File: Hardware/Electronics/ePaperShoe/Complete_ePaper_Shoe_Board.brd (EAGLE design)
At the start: 160 x 100 mm, 59 parts, among them Q1 IRF7509, U1 LM3671MF-3.3/NOPB, U2 NRF52832, U3 MCP73871, X1 32MHz, X2 32.768kHz, X3 FH12-26S-0.5SH

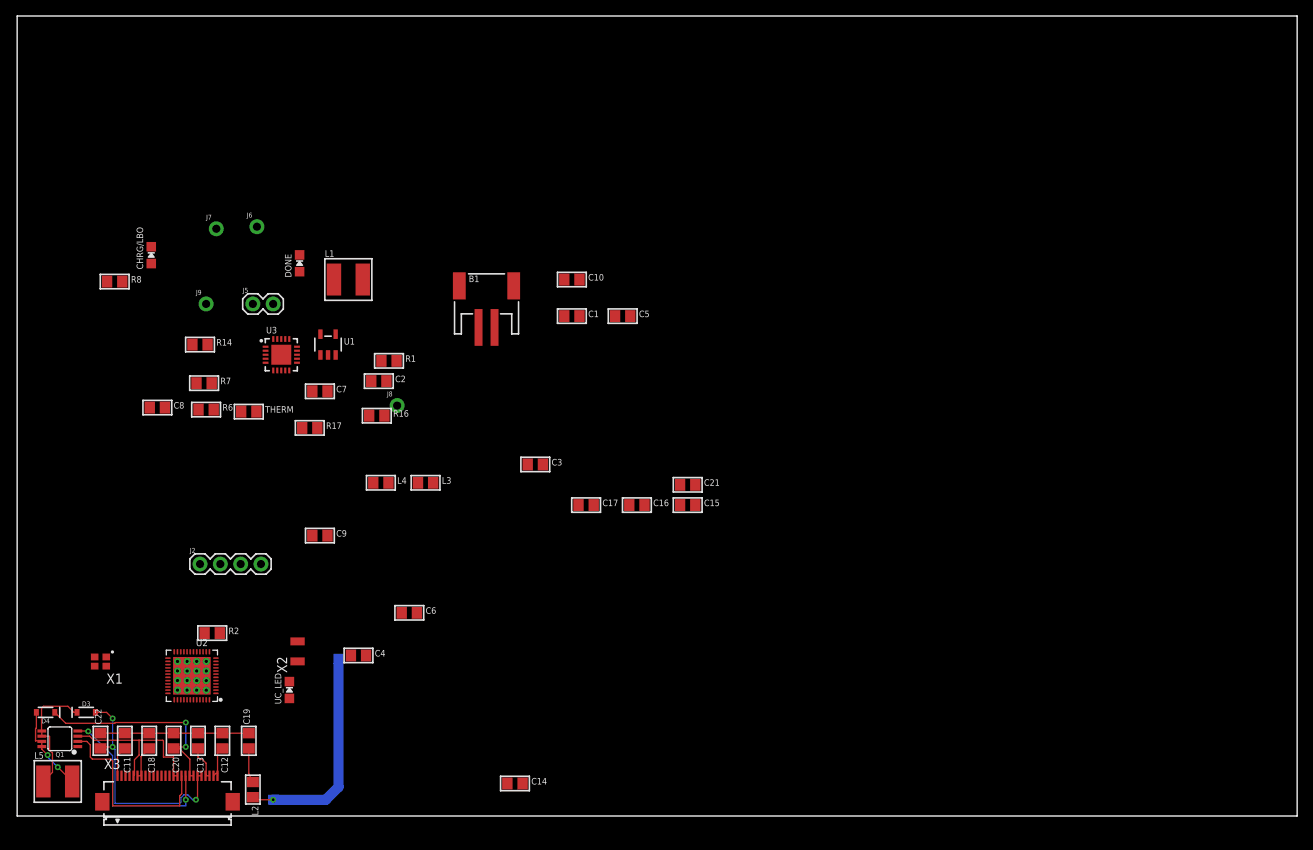
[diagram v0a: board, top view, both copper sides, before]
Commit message: Completed layout and traces of PCB. Need to still add silkscreen and arrange lables
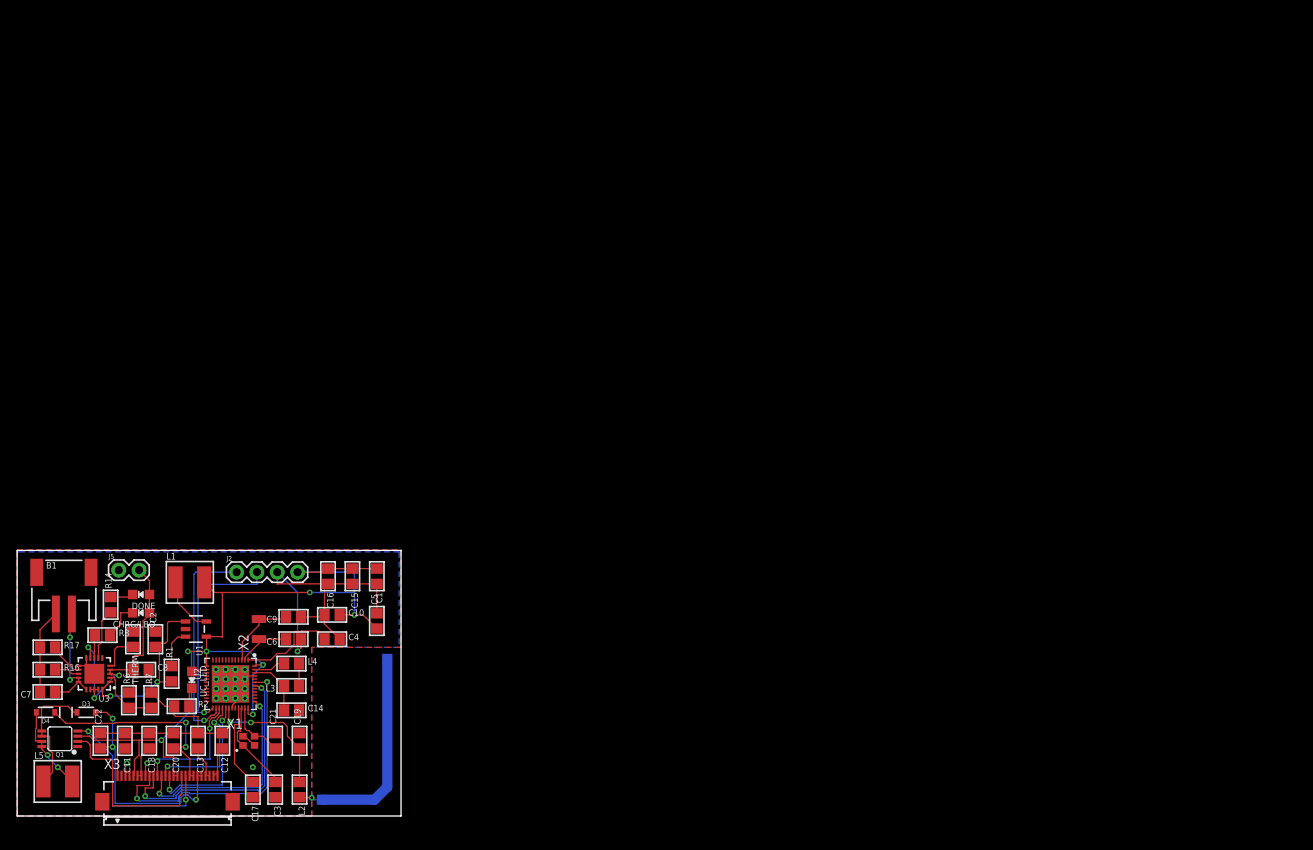
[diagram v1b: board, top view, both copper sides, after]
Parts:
- removed J6, J7, J8, J9: (no value), SparkFun-Connectors:1X01_NO_SILK
- moved FRAME1 81.9 mm to (-4.32, 23.1)
- moved B1 63.8 mm to (5.84, 29.0)
- moved C21 60.7 mm to (32.3, 9.40), turned to 90 degrees
- moved C17 54.8 mm to (29.5, 3.30), turned to 270 degrees
- moved C3 52.0 mm to (32.3, 3.30), turned to 270 degrees
- moved R16 52.0 mm to (3.81, 18.3)
- moved C10 51.5 mm to (39.4, 25.1)
- moved C7 50.7 mm to (3.81, 15.5), turned to 180 degrees
- moved C5 49.0 mm to (45.0, 24.4), turned to 90 degrees
- moved R1 47.6 mm to (19.3, 17.8), turned to 90 degrees
- moved U3 46.2 mm to (9.65, 17.8), turned to 180 degrees
- moved DONE 45.9 mm to (15.5, 27.7), turned to 90 degrees
- moved CHRG/LBO 44.7 mm to (15.5, 25.4), turned to 90 degrees
- moved R8 44.2 mm to (10.7, 22.6)
- moved C15 42.8 mm to (41.9, 30.0), turned to 270 degrees
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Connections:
- net 3.3V: no longer J7.1
- net GND: no longer J6.1
- net VBAT: no longer J8.1
- net VBUS: no longer J9.1
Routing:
- net GND: track 18.5 -> 121.6 mm, vias 0 -> 4
- net 3.3V: track 21.8 -> 112.6 mm, vias 0 -> 7
- net VBUS: track 0.00 -> 36.8 mm, vias 0 -> 3
- net P0.31: track 0.00 -> 36.7 mm, vias 0 -> 2
- net P0.30: track 0.00 -> 33.1 mm, vias 0 -> 2
- net SWDIO: track 0.00 -> 27.6 mm, vias 0 -> 1
- net SWDCLK: track 0.00 -> 27.1 mm, vias 0 -> 1
- net P0.25: track 0.00 -> 26.9 mm, vias 0 -> 2
- net VBAT: track 0.00 -> 22.6 mm, vias 0 -> 2
- net P0.24: track 0.00 -> 19.0 mm, vias 0 -> 2
- net P0.23: track 0.00 -> 16.4 mm, vias 0 -> 2
- net P0.22: track 0.00 -> 15.7 mm, vias 0 -> 2
- net VLIPO: track 0.00 -> 14.9 mm, vias 0 -> 2
- net ANT: track 4.32 -> 16.8 mm, vias 0 -> 2
- net DEC1: track 0.00 -> 12.4 mm
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- added copper zone on layer 1, net GND
- added copper zone on layer 16, net GND
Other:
- board size 160 x 100 mm -> 48 x 33.2 mm

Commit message: Completed PCB with everything on it V1.0
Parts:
- moved FRAME3 12.9 mm to (0.13, 33.4)
- moved FRAME1 11.2 mm to (0.00, 33.4)
- moved FRAME2 10.2 mm to (-0.13, 33.4)
- moved B1 0.92 mm to (5.33, 29.7)
- moved J2 0.25 mm to (27.4, 30.7)
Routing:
- net GND: track 121.6 -> 122.4 mm
- net VLIPO: track 14.9 -> 15.6 mm
- net 3.3V: track 112.6 -> 113.2 mm
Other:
- board text added: "3.3V"
- board text added: "5V IN"
- board text added: "Bioworld ePaper shoe"
- board text added: "Complete board for"
- board text added: "GND"
- board text added: "GND\"
- board text added: "Michael Currie"
- board text added: "SWDCLK"
- board text added: "SWDIO"
- board text added: "V1.0"

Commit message: Changes here and there, refining the product
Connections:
- net GND: now also J5.1
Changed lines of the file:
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@@
 <wire x1="28.4577125" y1="9.973" x2="29.1113125" y2="9.3194" width="0.1524" layer="1"/>
 <via x="29.464" y="6.096" extent="1-16" drill="0.35"/>
+<contactref element="J5" pad="1"/>
 <wire x1="27.108" y1="16.002" x2="26.67" y2="16.51" width="0" layer="19" extent="1-16"/>
 </signal>
